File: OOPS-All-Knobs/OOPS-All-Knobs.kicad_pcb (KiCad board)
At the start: 2 copper layers, 226.5 x 75 mm, 180 parts, among them J1 USB_C_Receptacle_USB2.0, J2 Conn_01x03_Female, SW1 SW_SPST, SW2 SW_SPST, U1 NCP1117-3.3_SOT223, U2 W25Q128JVS, U3 RP2040TR7, U4 SRV05-4, Y1 12MHz

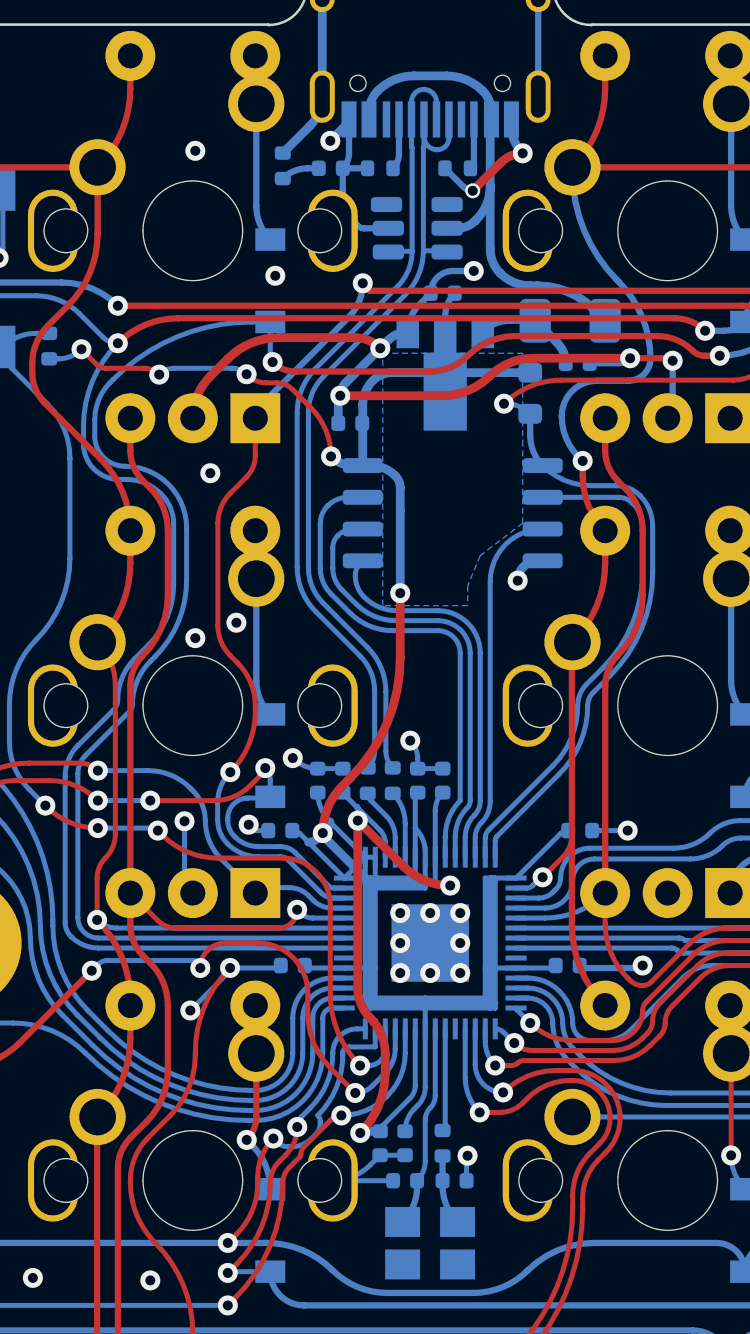
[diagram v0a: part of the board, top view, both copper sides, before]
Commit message: Implemented proposed fixes for testgen, shielding, and xtal
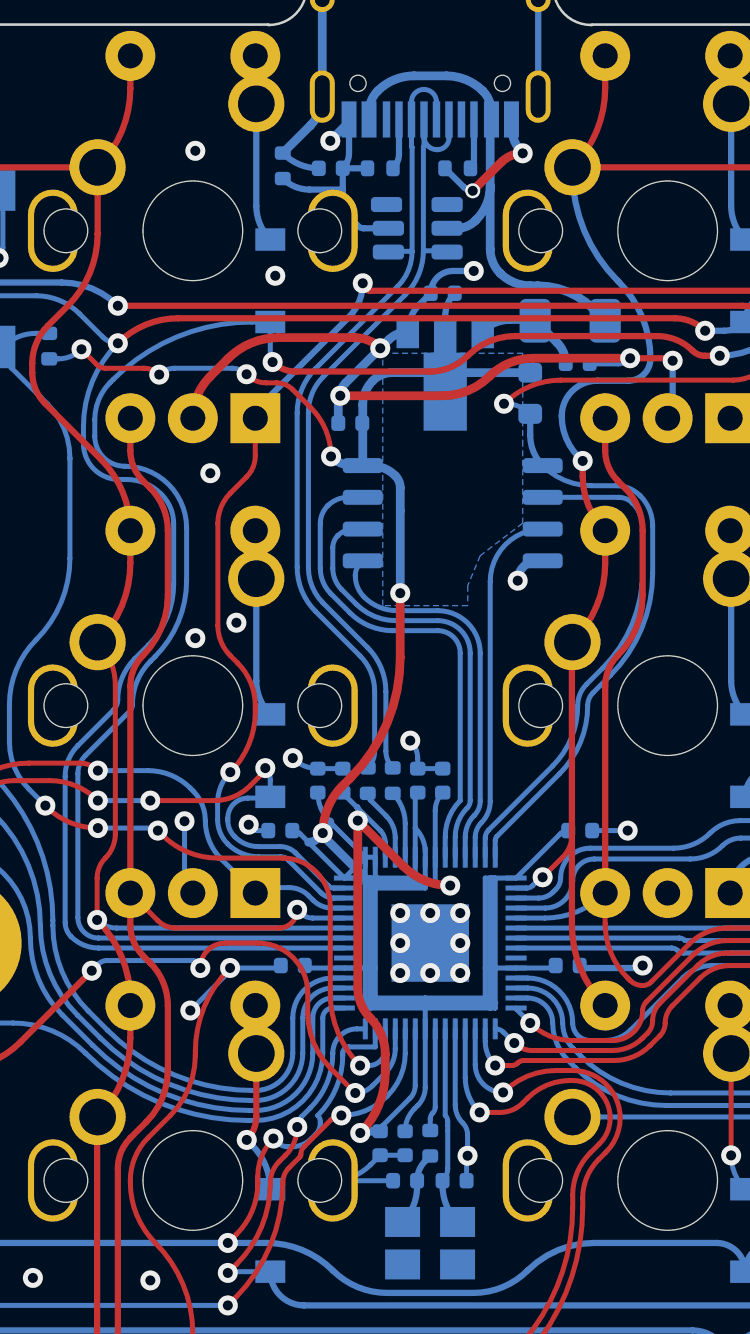
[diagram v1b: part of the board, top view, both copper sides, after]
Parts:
- C17: value 1u -> 10u
- C3: value 0.1u -> 4.7n
- moved R8 0.49 mm to (62.5, 64.5)
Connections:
- C3 pad 2: Net-(C3-Pad2) -> Net-(J1-PadS1)
- C5 pad 2: XOUT -> Net-(C5-Pad2)
- C6 pad 1: Net-(C6-Pad1) -> XIN
- R3 pad 1: Net-(C3-Pad2) -> GND
- R8 pad 1: Net-(C6-Pad1) -> Net-(C5-Pad2)
- R8 pad 2: XIN -> XOUT
- U3 pad 19: unconnected-(U3-Pad19) -> GND
- Y1 pad 1: XOUT -> Net-(C5-Pad2)
- Y1 pad 2: Net-(C6-Pad1) -> XIN
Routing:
- net GND: track 92.0 -> 99.7 mm
- net XOUT: track 8.05 -> 4.12 mm
- net XIN: track 4.09 -> 7.95 mm
- net Net-(C5-Pad2): track 0.00 -> 2.95 mm
- net Net-(C6-Pad1): track 2.79 -> 0.00 mm
- net Net-(J1-PadS1): track 19.8 -> 21.4 mm
- net Net-(C3-Pad2): track 1.54 -> 0.00 mm

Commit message: a few more improvements
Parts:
- added C15: 10u, Capacitor_SMD:C_0402_1005Metric, B.Cu at (63.2, 43.9)
- C17: value 10u -> 1u
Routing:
- net +3V3: track 136.9 -> 138.3 mm
- net QSPI_D3: track 19.1 -> 17.7 mm
- net QSPI_CLK: track 17.6 -> 16.2 mm
- net QSPI_D0: track 15.5 -> 14.2 mm
- net GND: track 99.7 -> 100.9 mm, vias 64 -> 65

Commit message: Gerbers ready for manu
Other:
- board text added: "RUN"
